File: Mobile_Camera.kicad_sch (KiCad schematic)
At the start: 26 parts, among them J1 SWD_header, J2 DVP_24_pin, J3 Micro_SD_card, SW1 SW_Power_On, SW2 SW_Reset, U1 STM32H753VIT6, Y1 Crystal

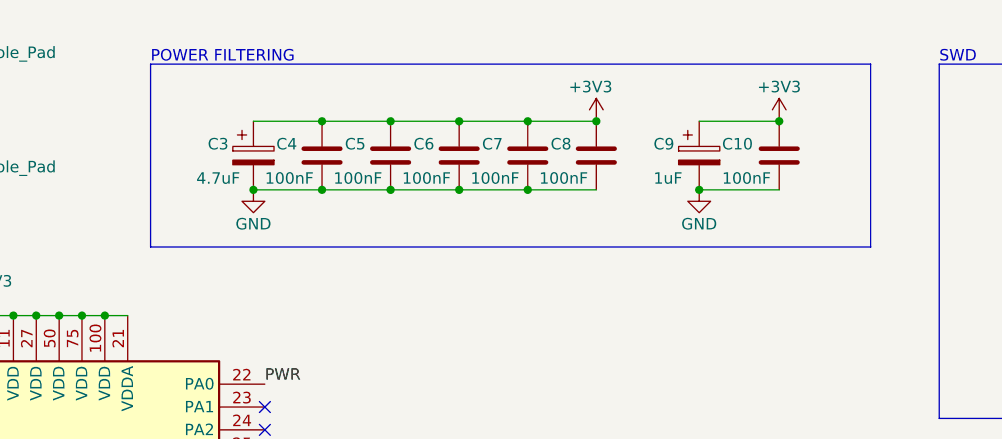
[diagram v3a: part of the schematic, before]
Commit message: Add power delivery routing
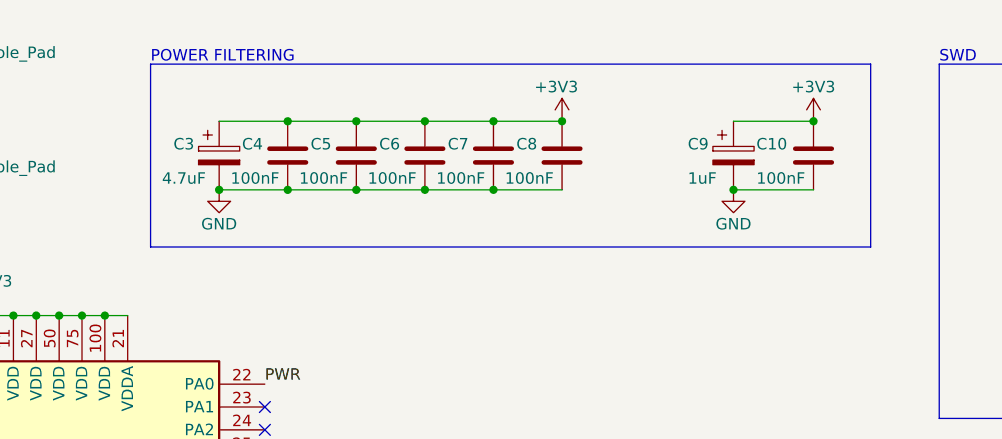
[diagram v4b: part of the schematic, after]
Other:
- moved on the sheet: C10, C3, C4, C5, C6, C7, C8, C9

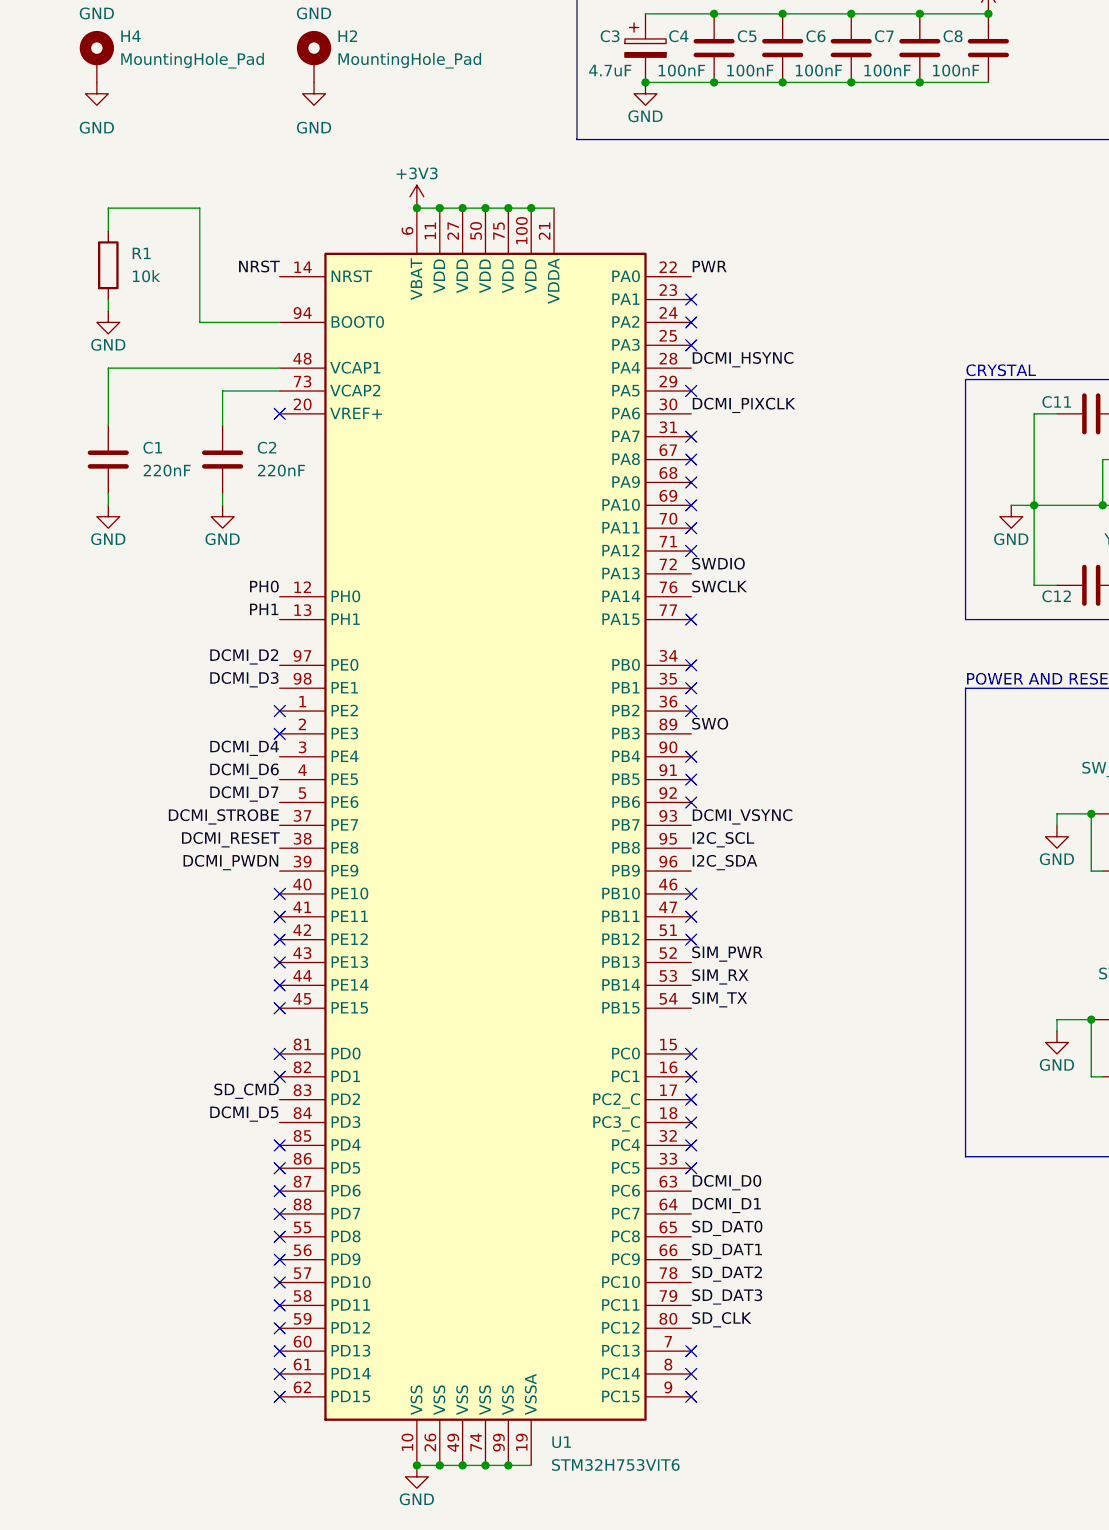
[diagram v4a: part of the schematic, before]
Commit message: Add controlled impedence trace
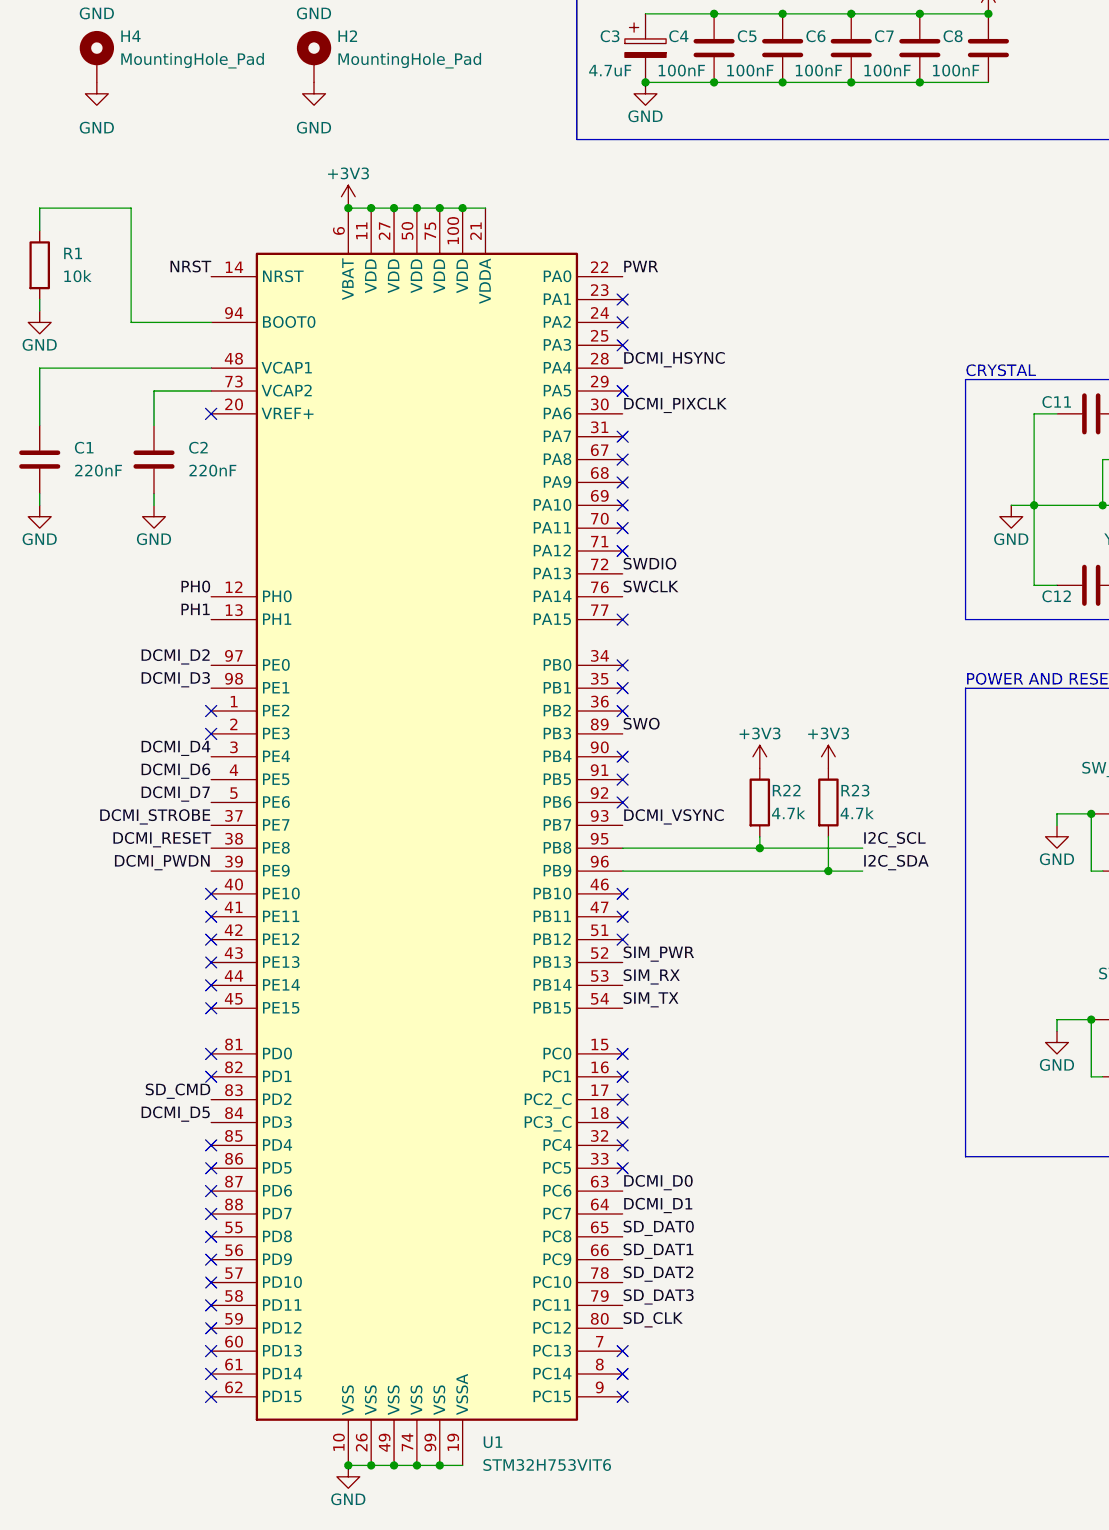
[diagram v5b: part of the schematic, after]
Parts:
- added R22, R23: 4.7k, Resistor_SMD:R_0603_1608Metric_Pad0.98x0.95mm_HandSolder, symbol Device:R
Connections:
- net +3V3: now also R22.1, R23.1
- net I2C_SCL: now also R22.2
- net I2C_SDA: now also R23.2
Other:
- moved on the sheet: C1, C2, R1, U1
